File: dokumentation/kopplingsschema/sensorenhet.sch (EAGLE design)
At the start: 6 parts

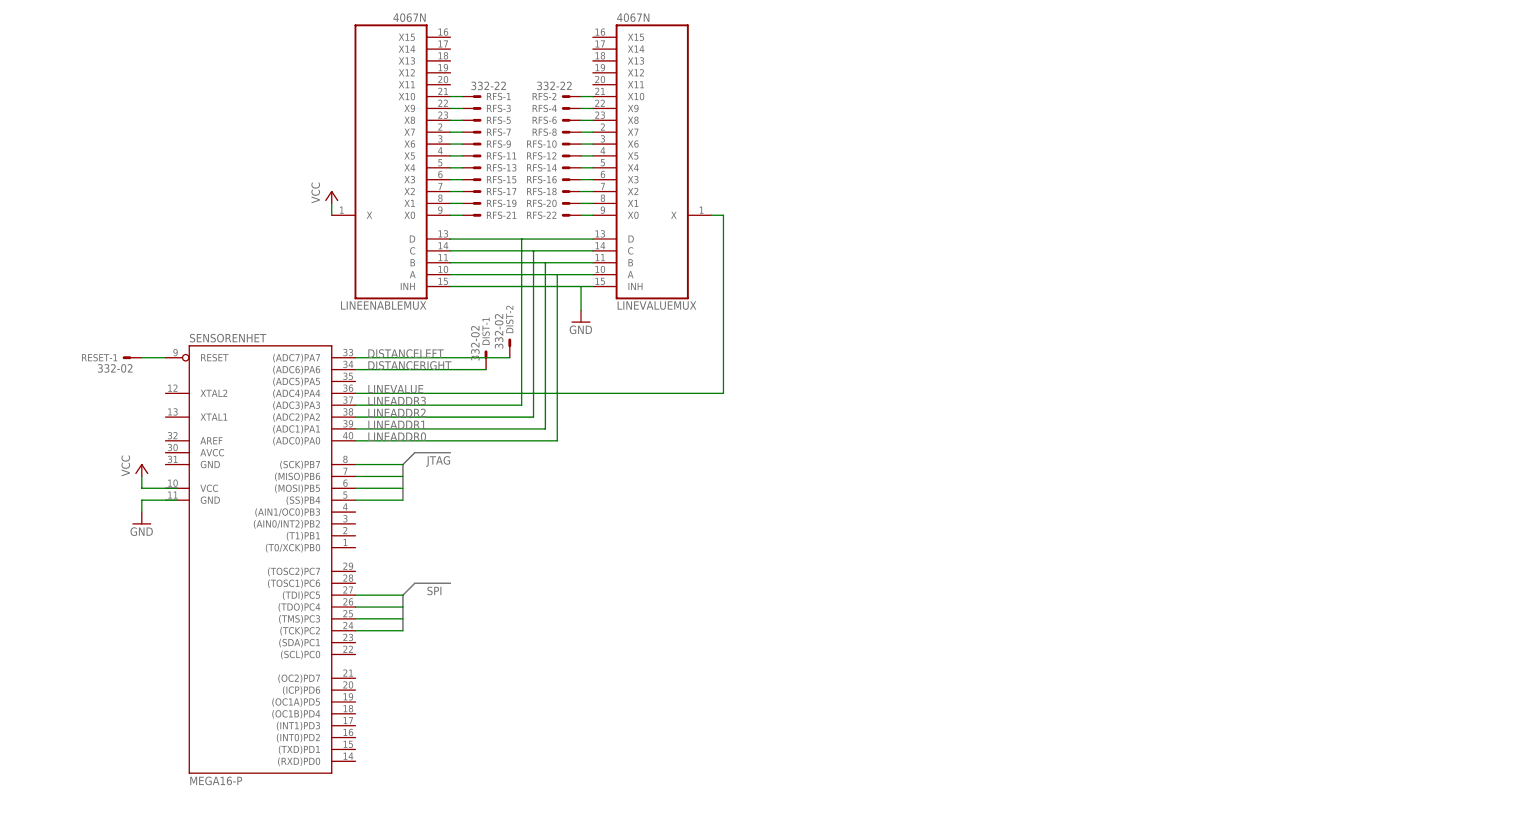
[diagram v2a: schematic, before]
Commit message: Updated circuit diagram of sensor unit.
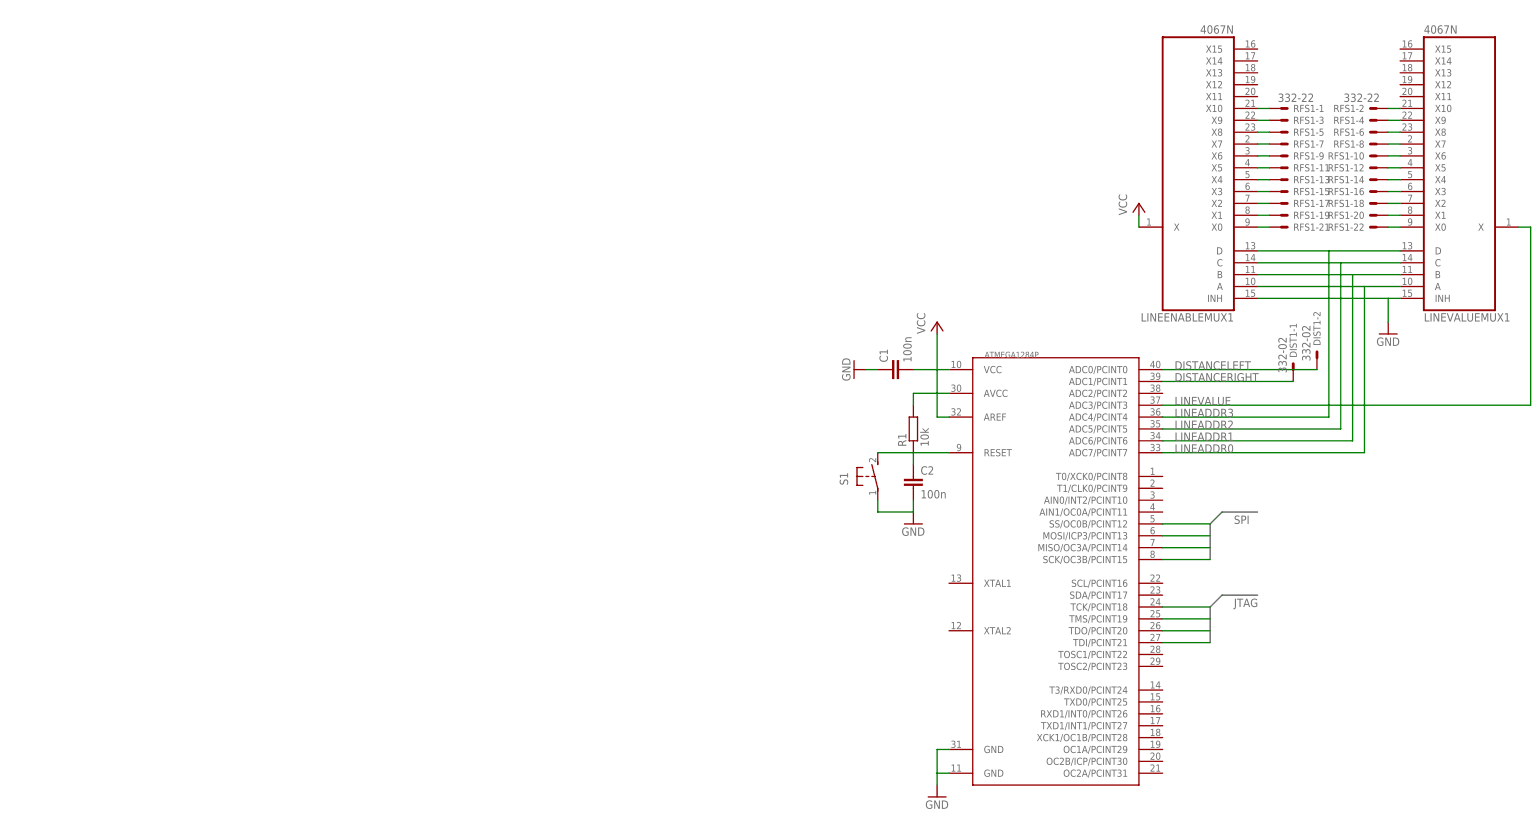
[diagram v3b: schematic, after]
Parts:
- removed DIST, RESET: 332-02, con-garry:332-02
- removed LINEENABLEMUX, LINEVALUEMUX: 4067N, 40xx:4067N
- removed RFS: 332-22, con-garry:332-22
- removed SENSORENHET: MEGA16-P, atmel:MEGA16-P
- added ATMEGA1284P: (no value), 1284p:MEGA1284P
- added C1, C2: 100n, rcl:C-EUC1206
- added DIST1: 332-02, con-garry:332-02
- added LINEENABLEMUX1, LINEVALUEMUX1: 4067N, 40xx:4067N
- added R1: 10k, resistor:R-EU_V235/17
- added RFS1: 332-22, con-garry:332-22
- added S1: (no value), switch-omron:31-XX
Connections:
- removed net N$1: SENSORENHET.(SS)PB4
- removed net N$10: LINEENABLEMUXA.X0, RFS-21.S
- removed net N$11: LINEENABLEMUXA.X1, RFS-19.S
- removed net N$12: LINEENABLEMUXA.X2, RFS-17.S
- removed net N$13: LINEENABLEMUXA.X3, RFS-15.S
- removed net N$14: LINEENABLEMUXA.X4, RFS-13.S
- removed net N$15: LINEENABLEMUXA.X5, RFS-11.S
- removed net N$16: LINEENABLEMUXA.X6, RFS-9.S
- removed net N$17: LINEENABLEMUXA.X7, RFS-7.S
- removed net N$18: LINEENABLEMUXA.X8, RFS-5.S
- removed net N$19: LINEENABLEMUXA.X9, RFS-3.S
- removed net N$2: SENSORENHET.(MOSI)PB5
- removed net N$20: LINEENABLEMUXA.X10, RFS-1.S
- removed net N$21: LINEVALUEMUXA.X10, RFS-2.S
- removed net N$22: LINEVALUEMUXA.X9, RFS-4.S
- removed net N$23: LINEVALUEMUXA.X8, RFS-6.S
- removed net N$24: LINEVALUEMUXA.X7, RFS-8.S
- removed net N$25: LINEVALUEMUXA.X6, RFS-10.S
- removed net N$26: LINEVALUEMUXA.X5, RFS-12.S
- removed net N$27: LINEVALUEMUXA.X4, RFS-14.S
- removed net N$28: LINEVALUEMUXA.X3, RFS-16.S
- removed net N$29: LINEVALUEMUXA.X2, RFS-18.S
- removed net N$3: SENSORENHET.(MISO)PB6
- removed net N$30: LINEVALUEMUXA.X1, RFS-20.S
- removed net N$31: LINEVALUEMUXA.X0, RFS-22.S
- removed net N$4: SENSORENHET.(SCK)PB7
- removed net N$5: RESET-1.S, SENSORENHET.RESET
- removed net N$6: SENSORENHET.(TDI)PC5
- removed net N$7: SENSORENHET.(TDO)PC4
- removed net N$8: SENSORENHET.(TMS)PC3
- removed net N$9: SENSORENHET.(TCK)PC2
- new net N$32: ATMEGA1284P.SCK/OC3B/PCINT15
- new net N$33: ATMEGA1284P.MISO/OC3A/PCINT14
- new net N$34: ATMEGA1284P.MOSI/ICP3/PCINT13
- new net N$35: ATMEGA1284P.SS/OC0B/PCINT12
- new net N$36: ATMEGA1284P.TCK/PCINT18
- new net N$37: ATMEGA1284P.TMS/PCINT19
- new net N$38: ATMEGA1284P.TDO/PCINT20
- new net N$39: ATMEGA1284P.TDI/PCINT21
- new net N$40: LINEENABLEMUX1A.X0, RFS1-21.S
- new net N$41: LINEENABLEMUX1A.X1, RFS1-19.S
- new net N$42: LINEENABLEMUX1A.X2, RFS1-17.S
- new net N$43: LINEENABLEMUX1A.X3, RFS1-15.S
- new net N$44: LINEENABLEMUX1A.X4, RFS1-13.S
- new net N$45: LINEENABLEMUX1A.X6, RFS1-9.S
- new net N$46: LINEENABLEMUX1A.X7, RFS1-7.S
- new net N$47: LINEENABLEMUX1A.X8, RFS1-5.S
- new net N$48: LINEENABLEMUX1A.X9, RFS1-3.S
- new net N$49: LINEENABLEMUX1A.X10, RFS1-1.S
- new net N$51: LINEENABLEMUX1A.X5, RFS1-11.S
- new net N$52: LINEVALUEMUX1A.X10, RFS1-2.S
- new net N$53: LINEVALUEMUX1A.X9, RFS1-4.S
- new net N$54: LINEVALUEMUX1A.X8, RFS1-6.S
- new net N$55: LINEVALUEMUX1A.X7, RFS1-8.S
- new net N$56: LINEVALUEMUX1A.X6, RFS1-10.S
- new net N$57: LINEVALUEMUX1A.X5, RFS1-12.S
- new net N$58: LINEVALUEMUX1A.X4, RFS1-14.S
- new net N$59: LINEVALUEMUX1A.X3, RFS1-16.S
- new net N$60: LINEVALUEMUX1A.X2, RFS1-18.S
- new net N$61: LINEVALUEMUX1A.X1, RFS1-20.S
- new net N$62: LINEVALUEMUX1A.X0, RFS1-22.S
- new net N$65: ATMEGA1284P.RESET, C2.1, R1.1, S1.S
- net DISTANCELEFT: now also ATMEGA1284P.ADC0/PCINT0, DIST1-2.S; no longer DIST-2.S, SENSORENHET.(ADC7)PA7
- net DISTANCERIGHT: now also ATMEGA1284P.ADC1/PCINT1, DIST1-1.S; no longer DIST-1.S, SENSORENHET.(ADC6)PA6
- net GND: now also ATMEGA1284P.GND@0, ATMEGA1284P.GND@1, C1.1, C2.2, LINEENABLEMUX1A.INH, LINEVALUEMUX1A.INH, S1.P; no longer LINEENABLEMUXA.INH, LINEVALUEMUXA.INH
- net LINEADDR0: now also ATMEGA1284P.ADC7/PCINT7, LINEENABLEMUX1A.A, LINEVALUEMUX1A.A; no longer LINEENABLEMUXA.A, LINEVALUEMUXA.A, SENSORENHET.(ADC0)PA0
- net LINEADDR1: now also ATMEGA1284P.ADC6/PCINT6, LINEENABLEMUX1A.B, LINEVALUEMUX1A.B; no longer LINEENABLEMUXA.B, LINEVALUEMUXA.B, SENSORENHET.(ADC1)PA1
- net LINEADDR2: now also ATMEGA1284P.ADC5/PCINT5, LINEENABLEMUX1A.C, LINEVALUEMUX1A.C; no longer LINEENABLEMUXA.C, LINEVALUEMUXA.C, SENSORENHET.(ADC2)PA2
- net LINEADDR3: now also ATMEGA1284P.ADC4/PCINT4, LINEENABLEMUX1A.D, LINEVALUEMUX1A.D; no longer LINEENABLEMUXA.D, LINEVALUEMUXA.D, SENSORENHET.(ADC3)PA3
- net LINEVALUE: now also ATMEGA1284P.ADC3/PCINT3, LINEVALUEMUX1A.X; no longer LINEVALUEMUXA.X, SENSORENHET.(ADC4)PA4
- net VCC: now also ATMEGA1284P.AREF, ATMEGA1284P.AVCC, ATMEGA1284P.VCC, C1.2, LINEENABLEMUX1A.X, R1.2; no longer LINEENABLEMUXA.X
